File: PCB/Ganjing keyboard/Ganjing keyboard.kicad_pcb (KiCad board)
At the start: 2 copper layers, 304.8 x 122.8 mm, 178 parts, among them J1 Conn_01x04, J2 AVR-ISP-6, SW1 Rotary_Encoder_Switch, U1 ATmega32A-PU, Y1 Crystal

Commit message: Enhancing readability of PCB
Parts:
- MX31: value Caps Lock -> ANSI Caps Lock
- MX43: value Enter -> ANSI Enter
- MX45: value Shift -> ANSI Shift
- MX59: value Ctrl -> 1.25u
- MX60: value Win -> 1.25u
- MX61: value Alt -> 1.25u
- MX62: value Space -> 6.25u
- MX72: value 1.5u Ctrl -> 1.5u
- MX73: value 1.5u Alt -> 1.5u
- MX74: value 7.00u Space -> 7.0u
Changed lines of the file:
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@@
     (mod_text_size 1 1)
     (mod_text_width 0.15)
-    (pad_size 4.4 4.4)
-    (pad_drill 2.2)
+    (pad_size 3.9878 3.9878)
+    (pad_drill 3.9878)
     (pad_to_mask_clearance 0.051)
     (solder_mask_min_width 0.25)
@@
     (descr "Alps rotary encoder, EC12E... with switch, vertical shaft, http://www.alps.com/prod/info/E/HTML/Encoder/Incremental/EC11/EC11E15204A3.html")
     (tags "rotary encoder")
-    (fp_text reference SW1 (at 2.8 -4.7 90) (layer F.SilkS)
+    (fp_text reference SW1 (at 7.39775 2.667 180) (layer F.SilkS)
       (effects (font (size 1 1) (thickness 0.15)))
     )
@@
       (effects (font (size 1 1) (thickness 0.15)))
     )
-    (fp_text value Space (at 0 -7.9375) (layer Dwgs.User)
+    (fp_text value 6.25u (at 0 -7.366) (layer F.SilkS)
       (effects (font (size 1 1) (thickness 0.15)))
     )
@@
       (effects (font (size 1 1) (thickness 0.15)))
     )
-    (fp_text value "ISO Enter" (at 0 -7.9375) (layer Dwgs.User)
+    (fp_text value "ISO Enter" (at 7.493 0.127 90) (layer F.SilkS)
       (effects (font (size 1 1) (thickness 0.15)))
     )
@@
       (effects (font (size 1 1) (thickness 0.15)))
     )
-    (fp_text value "7.00u Space" (at 0 -7.9375) (layer Dwgs.User)
+    (fp_text value 7.0u (at 0 -7.366) (layer F.SilkS)
       (effects (font (size 1 1) (thickness 0.15)))
     )
@@
       (effects (font (size 1 1) (thickness 0.15)))
     )
-    (fp_text value Enter (at 0 -7.9375) (layer Dwgs.User)
+    (fp_text value "ANSI Enter" (at 0 -7.62) (layer F.SilkS)
       (effects (font (size 1 1) (thickness 0.15)))
     )
@@
       (effects (font (size 1 1) (thickness 0.15)))
     )
-    (fp_text value Shift (at 0 -7.9375) (layer Dwgs.User)
+    (fp_text value "ANSI Shift" (at 0 -7.9375) (layer F.SilkS)
       (effects (font (size 1 1) (thickness 0.15)))
     )
@@
       (effects (font (size 1 1) (thickness 0.15)))
     )
-    (fp_text value "Stepped Caps Lock" (at 0.263 -6.9746) (layer Dwgs.User)
+    (fp_text value "Stepped Caps Lock" (at -4.826 4.572) (layer F.SilkS)
       (effects (font (size 1 1) (thickness 0.15)))
     )
@@
       (effects (font (size 1 1) (thickness 0.15)))
     )
-    (fp_text value "1.5u Alt" (at 0 -7.9375) (layer Dwgs.User)
+    (fp_text value 1.5u (at 0 4.572) (layer F.SilkS)
       (effects (font (size 1 1) (thickness 0.15)))
     )
@@
       (effects (font (size 1 1) (thickness 0.15)))
     )
-    (fp_text value "1.5u Ctrl" (at 0 -7.9375) (layer Dwgs.User)
+    (fp_text value 1.5u (at 0 4.572) (layer F.SilkS)
       (effects (font (size 1 1) (thickness 0.15)))
     )
@@
       (effects (font (size 1 1) (thickness 0.15)))
     )
-    (fp_text value "ISO Shift" (at 0 -7.9375) (layer Dwgs.User)
+    (fp_text value "ISO Shift" (at 0 4.318) (layer F.SilkS)
       (effects (font (size 1 1) (thickness 0.15)))
     )
@@
       (effects (font (size 1 1) (thickness 0.15)))
     )
-    (fp_text value "ISO #" (at 0 -7.9375) (layer Dwgs.User)
+    (fp_text value "ISO #" (at 0 4.572) (layer F.SilkS)
       (effects (font (size 1 1) (thickness 0.15)))
     )
@@
       (effects (font (size 1 1) (thickness 0.15)))
     )
-    (fp_text value "ISO \\" (at 0 -7.9375) (layer Dwgs.User)
+    (fp_text value "ISO \\" (at 0 4.318) (layer F.SilkS)
       (effects (font (size 1 1) (thickness 0.15)))
     )
@@
       (effects (font (size 1 1) (thickness 0.15)))
     )
-    (fp_text value Alt (at 0 -7.9375) (layer Dwgs.User)
+    (fp_text value 1.25u (at 0 -7.366) (layer F.SilkS)
       (effects (font (size 1 1) (thickness 0.15)))
     )
@@
       (effects (font (size 1 1) (thickness 0.15)))
     )
-    (fp_text value Win (at 0 -7.9375) (layer Dwgs.User)
+    (fp_text value 1.25u (at 0 -7.366) (layer F.SilkS)
       (effects (font (size 1 1) (thickness 0.15)))
     )
@@
       (effects (font (size 1 1) (thickness 0.15)))
     )
-    (fp_text value Ctrl (at 0 -7.9375) (layer Dwgs.User)
+    (fp_text value 1.25u (at 0 -7.366) (layer F.SilkS)
       (effects (font (size 1 1) (thickness 0.15)))
     )
@@
       (effects (font (size 1 1) (thickness 0.15)))
     )
-    (fp_text value "Caps Lock" (at 0 -7.9375) (layer Dwgs.User)
+    (fp_text value "ANSI Caps Lock" (at 0 -7.9375) (layer F.SilkS)
       (effects (font (size 1 1) (thickness 0.15)))
     )

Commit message: Fixing some formatting
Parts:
- MX31: value ANSI Caps Lock -> Standard
- MX69: value Stepped Caps Lock -> Stepped
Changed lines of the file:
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@@
       (effects (font (size 1 1) (thickness 0.15)))
     )
-    (fp_text value 6.25u (at 0 -7.366) (layer F.SilkS)
+    (fp_text value 6.25u (at 0 3.556) (layer F.SilkS)
       (effects (font (size 1 1) (thickness 0.15)))
     )
@@
       (effects (font (size 1 1) (thickness 0.15)))
     )
-    (fp_text value "ISO Enter" (at 7.493 0.127 90) (layer F.SilkS)
+    (fp_text value "ISO Enter" (at -0.127 5.461 180) (layer F.SilkS)
       (effects (font (size 1 1) (thickness 0.15)))
     )
@@
       (effects (font (size 1 1) (thickness 0.15)))
     )
-    (fp_text value 7.0u (at 0 -7.366) (layer F.SilkS)
+    (fp_text value 7.0u (at 0 3.556) (layer F.SilkS)
       (effects (font (size 1 1) (thickness 0.15)))
     )
@@
       (effects (font (size 1 1) (thickness 0.15)))
     )
-    (fp_text value "ANSI Shift" (at 0 -7.9375) (layer F.SilkS)
+    (fp_text value "ANSI Shift" (at 0 3.556) (layer F.SilkS)
       (effects (font (size 1 1) (thickness 0.15)))
     )
@@
       (effects (font (size 1 1) (thickness 0.15)))
     )
-    (fp_text value "Stepped Caps Lock" (at -4.826 4.572) (layer F.SilkS)
+    (fp_text value Stepped (at -5.842 3.556) (layer F.SilkS)
       (effects (font (size 1 1) (thickness 0.15)))
     )
@@
       (effects (font (size 1 1) (thickness 0.15)))
     )
-    (fp_text value 1.5u (at 0 4.572) (layer F.SilkS)
+    (fp_text value 1.5u (at 0 3.556) (layer F.SilkS)
       (effects (font (size 1 1) (thickness 0.15)))
     )
@@
       (effects (font (size 1 1) (thickness 0.15)))
     )
-    (fp_text value 1.5u (at 0 4.572) (layer F.SilkS)
+    (fp_text value 1.5u (at 0.85725 3.556) (layer F.SilkS)
       (effects (font (size 1 1) (thickness 0.15)))
     )
@@
       (effects (font (size 1 1) (thickness 0.15)))
     )
-    (fp_text value "ISO Shift" (at 0 4.318) (layer F.SilkS)
+    (fp_text value "ISO Shift" (at -0.0635 3.556) (layer F.SilkS)
       (effects (font (size 1 1) (thickness 0.15)))
     )
@@
       (effects (font (size 1 1) (thickness 0.15)))
     )
-    (fp_text value "ISO #" (at 0 4.572) (layer F.SilkS)
+    (fp_text value "ISO #" (at 0 3.556) (layer F.SilkS)
       (effects (font (size 1 1) (thickness 0.15)))
     )
@@
       (effects (font (size 1 1) (thickness 0.15)))
     )
-    (fp_text value "ISO \\" (at 0 4.318) (layer F.SilkS)
+    (fp_text value "ISO \\" (at 0 3.556) (layer F.SilkS)
       (effects (font (size 1 1) (thickness 0.15)))
     )
@@
       (effects (font (size 1 1) (thickness 0.15)))
     )
-    (fp_text value 1.25u (at 0 -7.366) (layer F.SilkS)
+    (fp_text value 1.25u (at 0 3.556) (layer F.SilkS)
       (effects (font (size 1 1) (thickness 0.15)))
     )
@@
       (effects (font (size 1 1) (thickness 0.15)))
     )
-    (fp_text value 1.25u (at 0 -7.366) (layer F.SilkS)
+    (fp_text value 1.25u (at 0 3.556) (layer F.SilkS)
       (effects (font (size 1 1) (thickness 0.15)))
     )
@@
       (effects (font (size 1 1) (thickness 0.15)))
     )
-    (fp_text value 1.25u (at 0 -7.366) (layer F.SilkS)
+    (fp_text value 1.25u (at -0.8255 3.556) (layer F.SilkS)
       (effects (font (size 1 1) (thickness 0.15)))
     )
@@
       (effects (font (size 1 1) (thickness 0.15)))
     )
-    (fp_text value "ANSI Caps Lock" (at 0 -7.9375) (layer F.SilkS)
-      (effects (font (size 1 1) (thickness 0.15)))
-    )
+    (fp_text value Standard (at 1.016 3.556) (layer F.SilkS)
+      (effects (font (size 1 1) (thickness 0.15)))
+    )

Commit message: Fixed firmware issues
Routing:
- net SW15A: track 324.8 -> 325.3 mm

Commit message: Fixing PCB error
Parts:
- D68: value Caps -> Caps lock
- MX31: value Standard -> Caps Lock
- MX43: value ANSI Enter -> Enter
- MX45: value ANSI Shift -> Shift
- MX59: value 1.25u -> Ctrl
- MX60: value 1.25u -> Win
- MX61: value 1.25u -> Alt
- MX62: value 6.25u -> Space
- MX69: value Stepped -> Stepped Caps Lock
- MX72: value 1.5u -> 1.5u Ctrl
- MX73: value 1.5u -> 1.5u Alt
- MX74: value 7.0u -> 7.00u Space
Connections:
- R1 pad 2: Boot -> Reset
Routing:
- net Boot: track 118.3 -> 35.2 mm
- net Reset: track 66.5 -> 109.5 mm

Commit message: Updating gerbers
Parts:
- D68: value Caps lock -> Caps
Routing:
- net Net-(D68-Pad1): track 26.3 -> 28.0 mm

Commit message: Fixing PCB error
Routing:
- net VCC: track 356.9 -> 358.4 mm

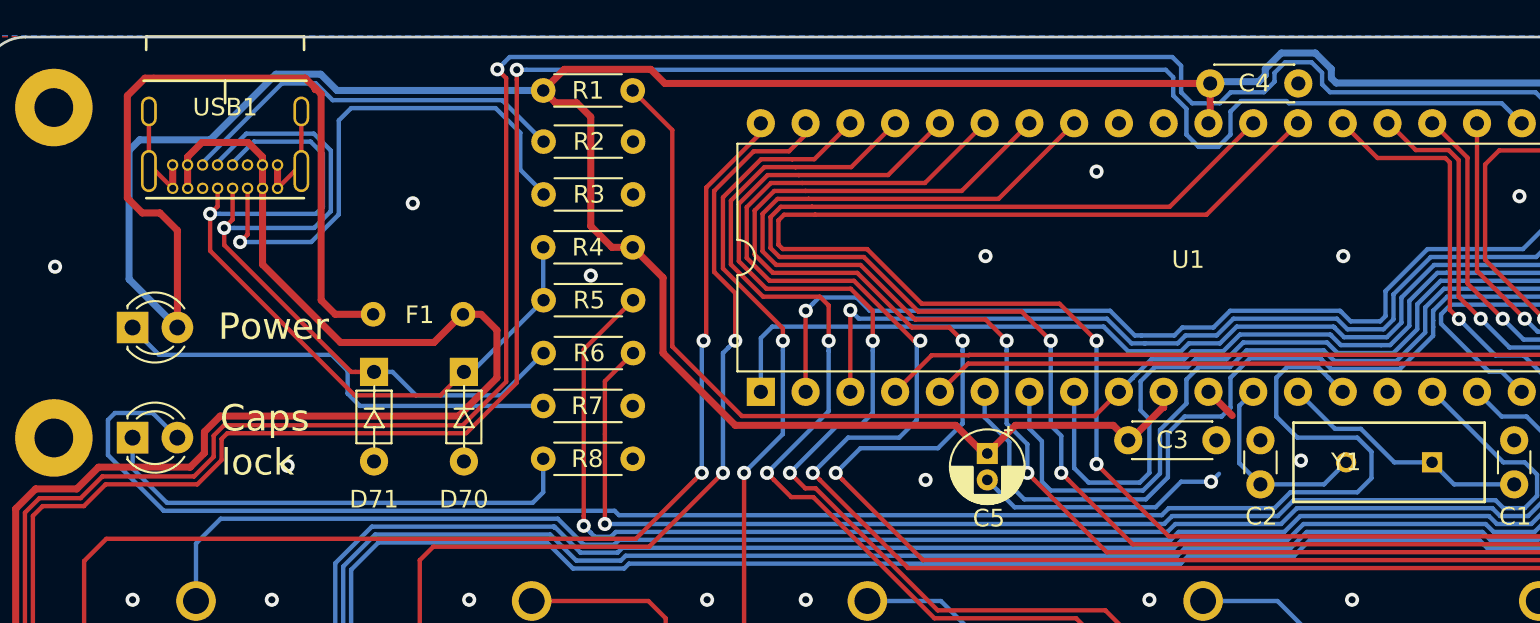
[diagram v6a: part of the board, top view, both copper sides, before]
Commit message: Removing caps lock LED
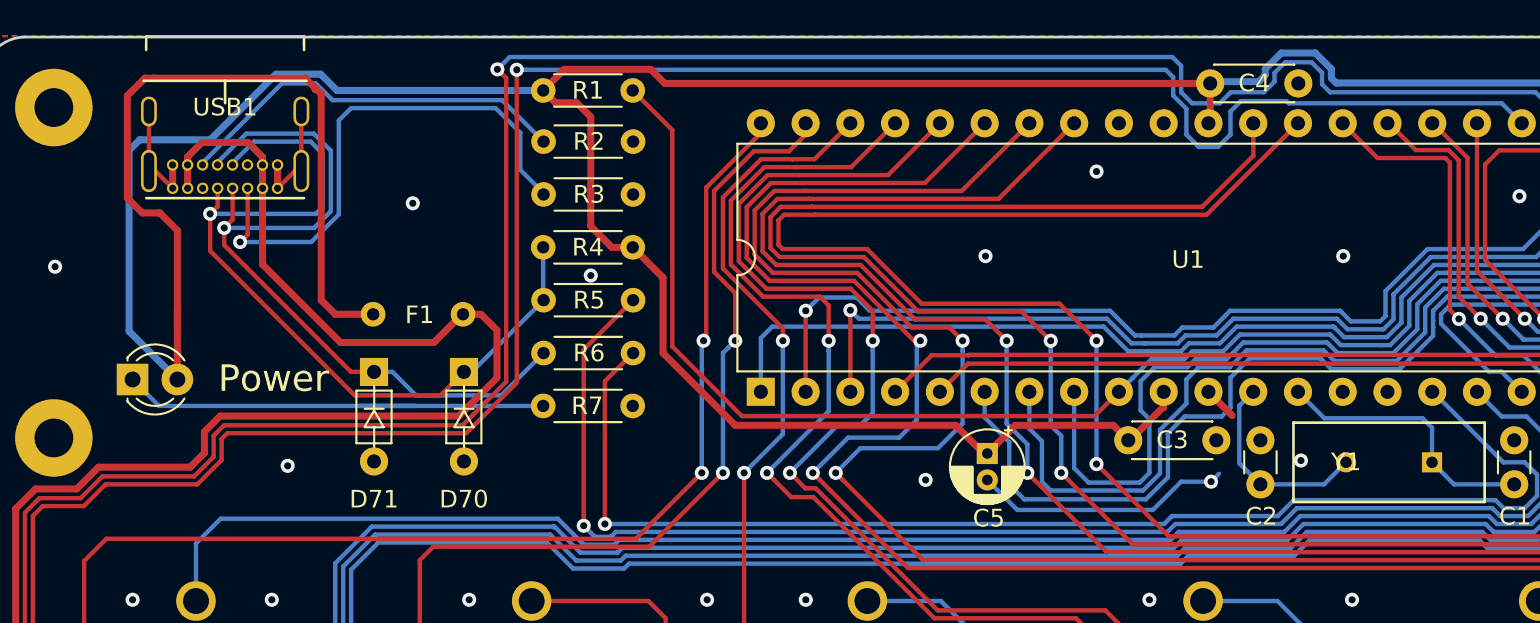
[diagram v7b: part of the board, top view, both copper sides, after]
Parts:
- removed D68: Caps, Keyboard:LED_D3.0mm
- removed R8: 62, Resistor_THT:R_Axial_DIN0204_L3.6mm_D1.6mm_P5.08mm_Horizontal
- moved D69 2.95 mm to (68.0, 115.7)
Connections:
- U1 pad 14: CapsLock -> Net-(U1-Pad14)
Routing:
- net CapsLock: track 95.2 -> 0.00 mm
- net Net-(D68-Pad1): track 28.0 -> 0.00 mm
- net +5V: track 236.1 -> 243.0 mm
- net Net-(C1-Pad1): track 14.5 -> 15.6 mm
- net col8: track 229.7 -> 230.8 mm
- net Net-(D69-Pad1): track 25.9 -> 27.0 mm

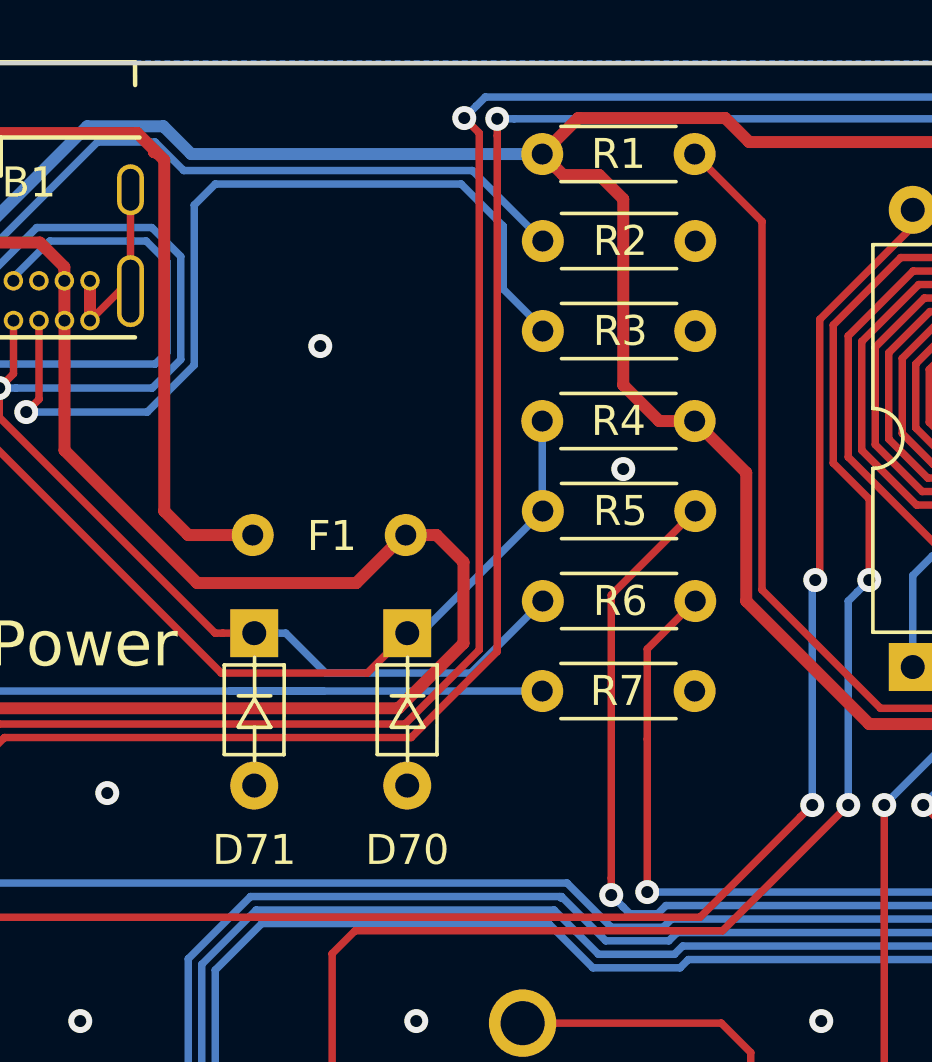
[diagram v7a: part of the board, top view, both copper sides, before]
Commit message: Updating images and generating new gerbers
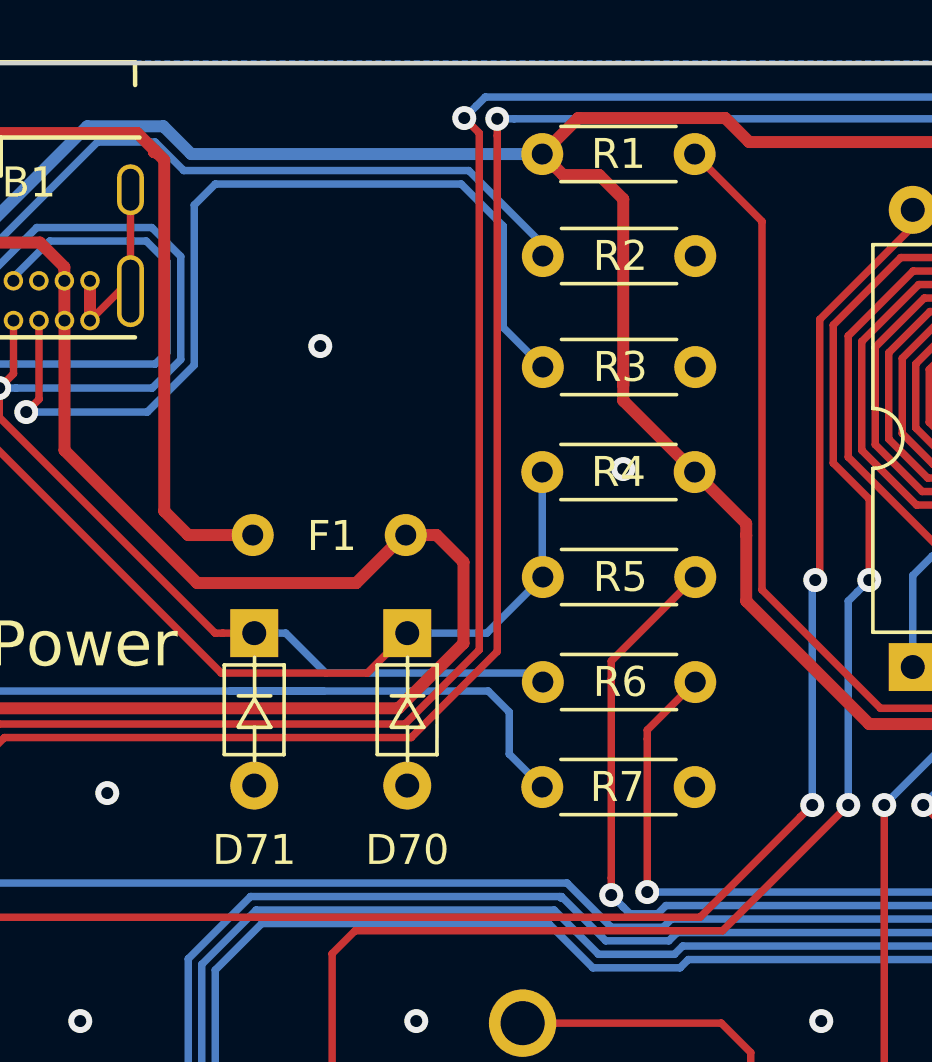
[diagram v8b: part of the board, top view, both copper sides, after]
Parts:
- moved R7 3.20 mm to (91.3, 120.4)
- moved R6 2.70 mm to (96.4, 116.9)
- moved R5 2.20 mm to (96.4, 113.4)
- moved R4 1.70 mm to (91.3, 109.9)
- moved R3 1.20 mm to (96.4, 106.4)
- moved R2 0.50 mm to (96.4, 102.7)
- renumbered D69 to D68
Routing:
- net D+: track 73.4 -> 70.7 mm
- net D-: track 78.5 -> 76.3 mm
- net Net-(D68-Pad1): track 27.0 -> 29.2 mm
- net Net-(R3-Pad2): track 30.0 -> 31.2 mm
- net Net-(D71-Pad1): track 43.6 -> 42.7 mm
